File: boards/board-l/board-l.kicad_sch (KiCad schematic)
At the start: 71 parts, among them J2 B6B-XH-A(LF)(SN), J3 SWD 1x5 (hand-fit), J4 UART pads, SW1 EC11 15-detent, U2 AL8860MP-13, U3 STM32G031F8P6, U4 AP63203WU-7

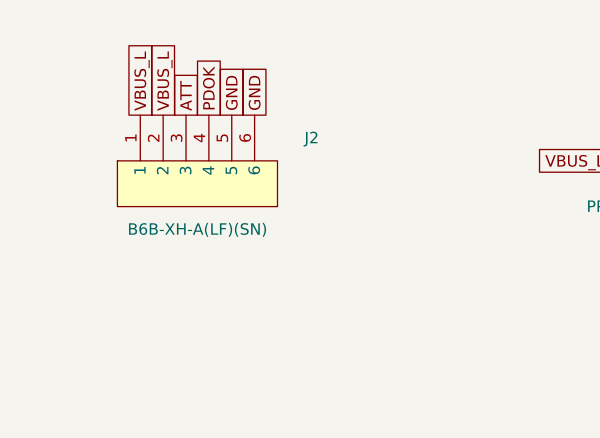
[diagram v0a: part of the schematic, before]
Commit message: feat(connectors): use XFCN board header pair
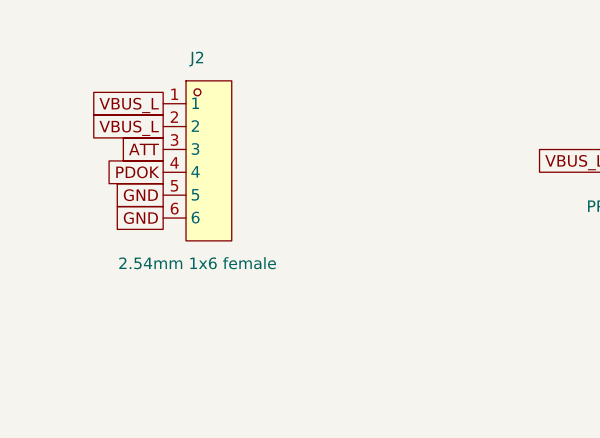
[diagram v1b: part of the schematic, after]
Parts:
- J2: value B6B-XH-A(LF)(SN) -> 2.54mm 1x6 female; footprint zudo-led-lamp:CONN-TH_6P-P2.50_B6B-XH-A-LF-SN -> zudo-led-lamp:HDR-TH_6P-P2.54-V-F; symbol zudo-led-lamp:B6B-XH-A -> zudo-led-lamp:PM254V-11-06-H85; LCSC C144397 -> C2832269
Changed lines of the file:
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@@
 	(paper "A2")
 	(symbol
-		(lib_id "zudo-led-lamp:B6B-XH-A")
+		(lib_id "zudo-led-lamp:PM254V-11-06-H85")
 		(at 38.1 50.8 0)
 		(unit 1)
@@
 		(dnp no)
 		(property "Reference" "J2"
-			(at 50.8 48.26 0)
+			(at 38.1 39.37 0)
 			(effects
 				(font (size 1.27 1.27))
 			)
 		)
-		(property "Value" "B6B-XH-A(LF)(SN)"
-			(at 38.1 58.42 0)
+		(property "Value" "2.54mm 1x6 female"
+			(at 38.1 62.23 0)
 			(effects
 				(font (size 1.27 1.27))
 			)
 		)
-		(property "Footprint" "zudo-led-lamp:CONN-TH_6P-P2.50_B6B-XH-A-LF-SN"
+		(property "Footprint" "zudo-led-lamp:HDR-TH_6P-P2.54-V-F"
 			(at 38.1 50.8 0)
 			(effects
@@
 			)
 		)
-		(property "LCSC" "C144397"
+		(property "LCSC" "C2832269"
 			(at 38.1 58.42 0)
 			(effects
@@
 	(global_label "VBUS_L"
 		(shape passive)
-		(at 31.75 45.72 90)
+		(at 34.29 44.45 180)
 		(effects
 			(font (size 1.27 1.27))
-			(justify left)
+			(justify right)
 		)
 	)
 	(global_label "VBUS_L"
 		(shape passive)
-		(at 34.29 45.72 90)
+		(at 34.29 46.99 180)
 		(effects
 			(font (size 1.27 1.27))
-			(justify left)
+			(justify right)
 		)
 	)
@@
 	(global_label "PDOK"
 		(shape passive)
-		(at 39.37 45.72 90)
+		(at 34.29 52.07 180)
 		(effects
 			(font (size 1.27 1.27))
-			(justify left)
+			(justify right)
 		)
 	)
@@
 	(global_label "ATT"
 		(shape passive)
-		(at 36.83 45.72 90)
+		(at 34.29 49.53 180)
 		(effects
 			(font (size 1.27 1.27))
-			(justify left)
+			(justify right)
 		)
 	)
@@
 	(global_label "GND"
 		(shape passive)
-		(at 41.91 45.72 90)
+		(at 34.29 54.61 180)
 		(effects
 			(font (size 1.27 1.27))
-			(justify left)
+			(justify right)
 		)
 	)
 	(global_label "GND"
 		(shape passive)
-		(at 44.45 45.72 90)
+		(at 34.29 57.15 180)
 		(effects
 			(font (size 1.27 1.27))
-			(justify left)
+			(justify right)
 		)
 	)

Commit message: Add WR11AS external lamp power rocker and assembly documentation
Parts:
- added J5: Power switch solder pads, zudo-led-lamp:SolderWire_1x02_P5.08mm, symbol zudo-led-lamp:Conn_1x02
- added SW2: WR11AS (panel rocker), symbol zudo-led-lamp:WR11AS
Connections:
- net V15: now also J5.2, SW2.1b; no longer F1.2
- new net V15_FUSED: F1.2, J5.1, SW2.1a
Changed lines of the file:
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@@
 	(paper "A2")
 	(symbol
+		(lib_id "zudo-led-lamp:WR11AS")
+		(at 444.5 50.8 0)
+		(unit 1)
+		(exclude_from_sim no)
+		(in_bom yes)
+		(on_board no)
+		(dnp no)
+		(property "Reference" "SW2"
+			(at 444.5 45.72 0)
+			(effects
+				(font (size 1.27 1.27))
+			)
+		)
+		(property "Value" "WR11AS (panel rocker)"
+			(at 444.5 55.88 0)
+			(effects
+				(font (size 1.27 1.27))
+			)
+		)
+		(property "Footprint" ""
+			(at 444.5 50.8 0)
+			(effects
+				(font (size 1.27 1.27))
+				(hide yes)
+			)
+		)
+		(property "Datasheet" "https://www.nkkswitches.com/pdf/WR.pdf"
+			(at 444.5 50.8 0)
+			(effects
+				(font (size 1.27 1.27))
+				(hide yes)
+			)
+		)
+		(property "MPN" "WR11AS"
+			(at 444.5 50.8 0)
+			(effects
+				(font (size 1.27 1.27))
+				(hide yes)
+			)
+		)
+		(property "Manufacturer" "NKK Switches"
+			(at 444.5 50.8 0)
+			(effects
+				(font (size 1.27 1.27))
+				(hide yes)
+			)
+		)
+		(property "Supplier" "DigiKey"
+			(at 444.5 50.8 0)
+			(effects
+				(font (size 1.27 1.27))
+				(hide yes)
+			)
+		)
+		(property "Supplier Part" "360-1507-ND"
+			(at 444.5 50.8 0)
+			(effects
+				(font (size 1.27 1.27))
+				(hide yes)
+			)
+		)
+		(property "Assembly" "External panel mount; hand wire via J5"
+			(at 444.5 50.8 0)
+			(effects
+				(font (size 1.27 1.27))
+				(hide yes)
+			)
+		)
+		(pin "1a"
+		)
+		(pin "1b"
+		)
+		(instances
+			(project "board-l"
+				(path "/ef98bbc0-7939-597a-8146-6f278c102a15"
+					(reference "SW2")
+					(unit 1)
+				)
+			)
+		)
+	)
+	(symbol
+		(lib_id "zudo-led-lamp:Conn_1x02")
+		(at 444.5 101.6 0)
+		(unit 1)
+		(exclude_from_sim no)
+		(in_bom no)
+		(on_board yes)
+		(dnp no)
+		(property "Reference" "J5"
+			(at 444.5 95.25 0)
+			(effects
+				(font (size 1.27 1.27))
+			)
+		)
+		(property "Value" "Power switch solder pads"
+			(at 444.5 107.95 0)
+			(effects
+				(font (size 1.27 1.27))
+			)
+		)
+		(property "Footprint" "zudo-led-lamp:SolderWire_1x02_P5.08mm"
+			(at 444.5 101.6 0)
+			(effects
+				(font (size 1.27 1.27))
+				(hide yes)
+			)
+		)
+		(property "Datasheet" ""
+			(at 444.5 101.6 0)
+			(effects
+				(font (size 1.27 1.27))
+				(hide yes)
+			)
+		)
+		(pin "1"
+		)
+		(pin "2"
+		)
+		(instances
+			(project "board-l"
+				(path "/ef98bbc0-7939-597a-8146-6f278c102a15"
+					(reference "J5")
+					(unit 1)
+				)
+			)
+		)
+	)
+	(symbol
 		(lib_id "zudo-led-lamp:PM254V-11-06-H85")
 		(at 38.1 50.8 0)
@@
 		)
 	)
-	(global_label "V15"
+	(global_label "V15_FUSED"
 		(shape passive)
 		(at 93.98 50.8 0)
@@
 		)
 	)
+	(global_label "V15_FUSED"
+		(shape passive)
+		(at 439.42 100.33 180)
+		(effects
+			(font (size 1.27 1.27))
+			(justify right)
+		)
+	)
+	(global_label "V15_FUSED"
+		(shape passive)
+		(at 436.88 50.8 180)
+		(effects
+			(font (size 1.27 1.27))
+			(justify right)
+		)
+	)
+	(global_label "V15"
+		(shape passive)
+		(at 452.12 50.8 0)
+		(effects
+			(font (size 1.27 1.27))
+			(justify left)
+		)
+	)
+	(global_label "V15"
+		(shape passive)
+		(at 439.42 102.87 180)
+		(effects
+			(font (size 1.27 1.27))
+			(justify right)
+		)
+	)
